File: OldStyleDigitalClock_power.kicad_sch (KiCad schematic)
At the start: 23 parts, among them J1 USB_A_OUT, J2 USB_A_OUT, J3 USB_C_IN, U11 NA555P

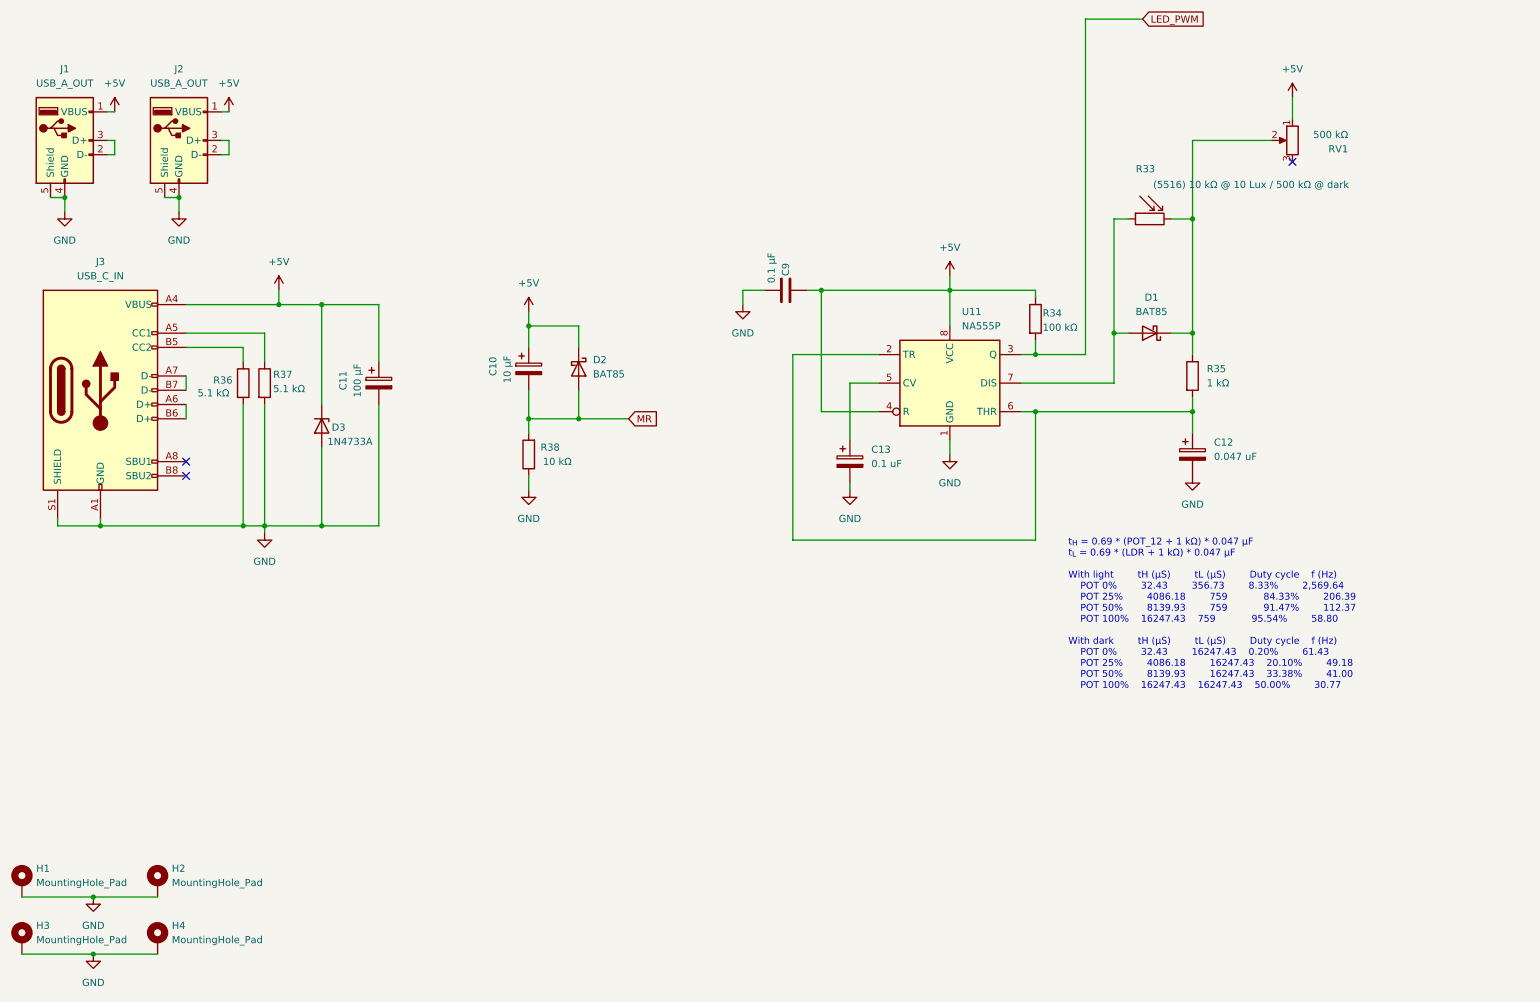
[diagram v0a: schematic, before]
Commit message: Constant frequency PWM with fixed LDR value
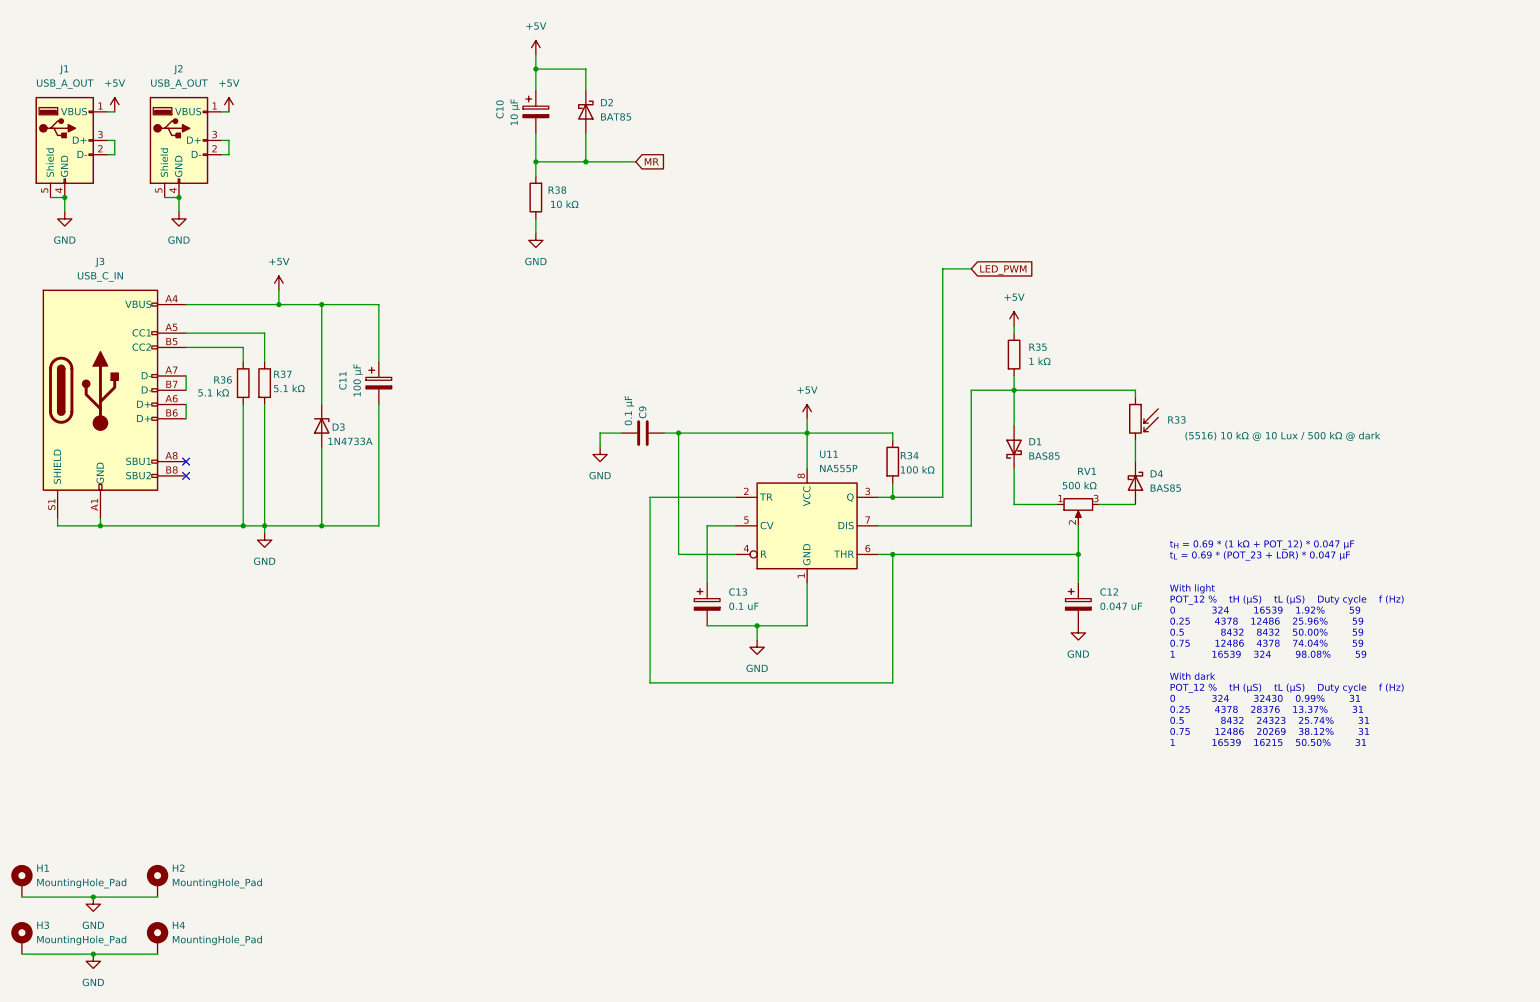
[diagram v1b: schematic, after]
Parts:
- added D4: BAS85, Diode_THT:D_DO-35_SOD27_P7.62mm_Horizontal, symbol Diode:BAT85
- D1: value BAT85 -> BAS85
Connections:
- net +5V: now also R35.1; no longer RV1.1
- net at C12.1, U11.2 (TR), U11.6 (THR): now also RV1.2; no longer R35.2
- net at RV1.3: now also D4.2 (A)
- net at D1.2 (A), R33.1, U11.7 (DIS): now also R35.2
- new net: D1.1 (K), RV1.1
- new net: D4.1 (K), R33.2
- no-connect marks 3 -> 2
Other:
- note added: "t_{H} = 0.69 * (1 kΩ + POT_12) * 0.047 µF t_{L} = 0.69 * (POT_23 + LDR) * 0.047 µF With light POT_12 % tH (µS) tL (µS) Duty cycle f (Hz) 0 324 16539 1.92% 59 0.25 4378 12486 25.96% 59 0.5 8432 8432 50.00% 59 0.75 12486 4378 74.04% 59 1 16539 324 98.08% 59 With dark POT_12 % tH (µS) tL (µS) Duty cycle f (Hz) 0 324 32430 0.99% 31 0.25 4378 28376 13.37% 31 0.5 8432 24323 25.74% 31 0.75 12486 20269 3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"
- note removed: "t_{H} = 0.69 * (POT_12 + 1 kΩ) * 0.047 µF t_{L} = 0.69 * (LDR + 1 kΩ) * 0.047 µF With light tH (µS) tL (µS) Duty cycle f (Hz) POT 0% 32.43 356.73 8.33% 2,569.64 POT 25% 4086.18 759 84.33% 206.39 POT 50% 8139.93 759 91.47% 112.37 POT 100% 16247.43 759 95.54% 58.80 With dark tH (µS) tL (µS) Duty cycle f (Hz) POT 0% 32.43 16247.43 0.20% 61.43 POT 25% 4086.18 16247.43 20.10% 49.18 POT 50% 8139.93 162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"
- moved on the sheet: C10, C12, C13, C9, D1, D2, R33, R34, R35, R38, RV1, U11

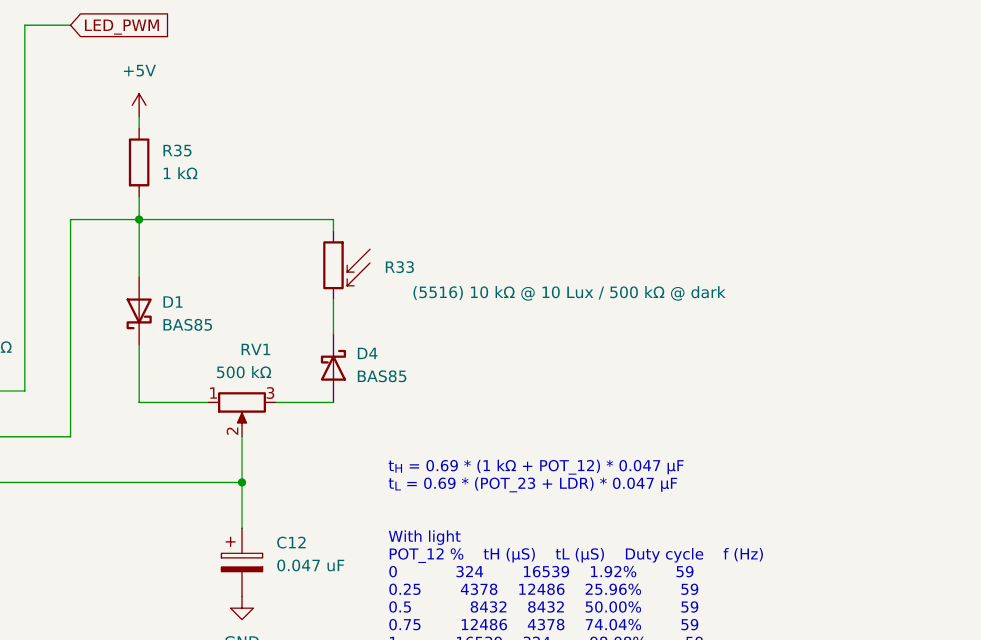
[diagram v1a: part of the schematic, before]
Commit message: Fixed typo
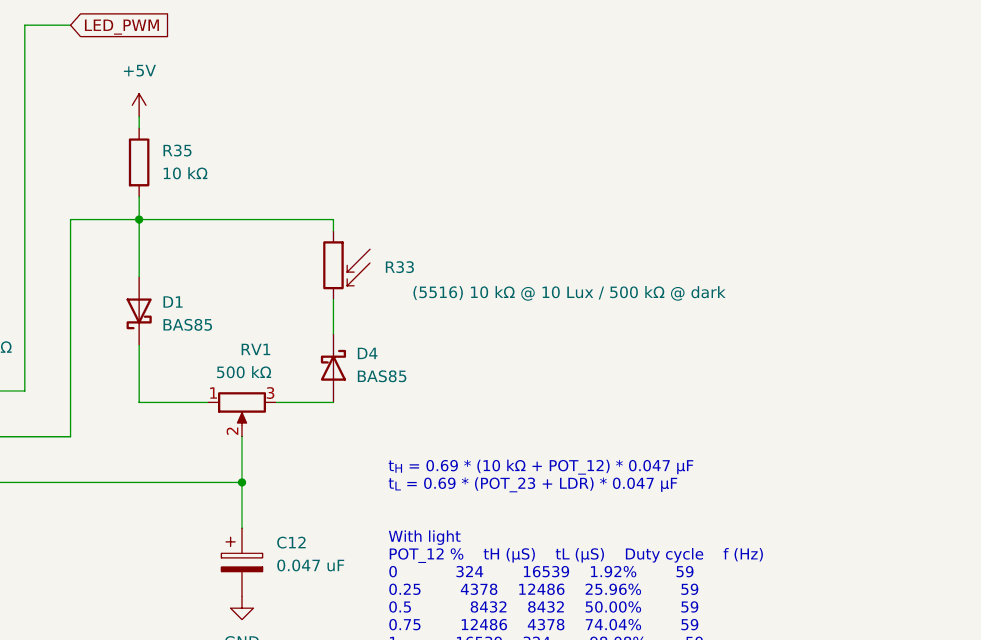
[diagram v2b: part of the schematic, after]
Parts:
- R35: value 1 kΩ -> 10 kΩ
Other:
- note added: "t_{H} = 0.69 * (10 kΩ + POT_12) * 0.047 µF t_{L} = 0.69 * (POT_23 + LDR) * 0.047 µF With light POT_12 % tH (µS) tL (µS) Duty cycle f (Hz) 0 324 16539 1.92% 59 0.25 4378 12486 25.96% 59 0.5 8432 8432 50.00% 59 0.75 12486 4378 74.04% 59 1 16539 324 98.08% 59 With dark POT_12 % tH (µS) tL (µS) Duty cycle f (Hz) 0 324 32430 0.99% 31 0.25 4378 28376 13.37% 31 0.5 8432 24323 25.74% 31 0.75 12486 20269 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"
- note removed: "t_{H} = 0.69 * (1 kΩ + POT_12) * 0.047 µF t_{L} = 0.69 * (POT_23 + LDR) * 0.047 µF With light POT_12 % tH (µS) tL (µS) Duty cycle f (Hz) 0 324 16539 1.92% 59 0.25 4378 12486 25.96% 59 0.5 8432 8432 50.00% 59 0.75 12486 4378 74.04% 59 1 16539 324 98.08% 59 With dark POT_12 % tH (µS) tL (µS) Duty cycle f (Hz) 0 324 32430 0.99% 31 0.25 4378 28376 13.37% 31 0.5 8432 24323 25.74% 31 0.75 12486 20269 3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"
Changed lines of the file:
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@@
 		(company "Pasquale Lafiosca")
 	)
-	(text "t_{H} = 0.69 * (1 kΩ + POT_12) * 0.047 µF\nt_{L} = 0.69 * (POT_23 + LDR) * 0.047 µF\n\n\nWith light				\nPOT_12 %	tH (µS)	tL (µS)	Duty cycle	f (Hz)\n0			324		16539	1.92%		59\n0.25		4378	12486	25.96%		59\n0.5			8432	8432	50.00%		59\n0.75		12486	4378	74.04%		59\n1			16539	324		98.08%		59\n				\nWith dark				\nPOT_12 %	tH (µS)	tL (µS)	Duty cycle	f (Hz)\n0			324		32430	0.99%		31\n0.25		4378	28376	13.37%		31\n0.5			8432	24323	25.74%		31\n0.75		12486	20269	38.12%		31\n1			16539	16215	50.50%		31\n"
+	(text "t_{H} = 0.69 * (10 kΩ + POT_12) * 0.047 µF\nt_{L} = 0.69 * (POT_23 + LDR) * 0.047 µF\n\n\nWith light				\nPOT_12 %	tH (µS)	tL (µS)	Duty cycle	f (Hz)\n0			324		16539	1.92%		59\n0.25		4378	12486	25.96%		59\n0.5			8432	8432	50.00%		59\n0.75		12486	4378	74.04%		59\n1			16539	324		98.08%		59\n				\nWith dark				\nPOT_12 %	tH (µS)	tL (µS)	Duty cycle	f (Hz)\n0			324		32430	0.99%		31\n0.25		4378	28376	13.37%		31\n0.5			8432	24323	25.74%		31\n0.75		12486	20269	38.12%		31\n1			16539	16215	50.50%		31\n"
 		(exclude_from_sim no)
 		(at 229.616 112.014 0)
@@
 			)
 		)
-		(property "Value" "1 kΩ"
+		(property "Value" "10 kΩ"
 			(at 204.47 80.0099 0)
 			(effects

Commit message: Assigned footprints: first draft
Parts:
- removed U11: NA555P, Package_DIP:DIP-8_W7.62mm, symbol Timer:NA555P
- added U12: NE555D, Package_SO:SOIC-8_3.9x4.9mm_P1.27mm, symbol Timer:NE555D
- RV1: footprint Resistor_SMD:R_1206_3216Metric -> Potentiometer_THT:Potentiometer_Alps_RK163_Single_Horizontal
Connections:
- net +5V: now also U12.4 (R), U12.8 (VCC)
- net GND: now also U12.1 (GND)
- net LED_PWM: now also U12.3 (Q)
- net at C12.1, RV1.2: now also U12.2 (TR), U12.6 (THR)
- net at D1.2 (A), R33.1, R35.2: now also U12.7 (DIS)
- net at C13.1: now also U12.5 (CV)
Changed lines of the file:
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@@
 			)
 		)
-		(property "Footprint" "Resistor_SMD:R_1206_3216Metric"
+		(property "Footprint" "Potentiometer_THT:Potentiometer_Alps_RK163_Single_Horizontal"
 			(at 213.36 105.41 0)
 			(effects
@@
 	)
 	(symbol
-		(lib_id "Timer:NA555P")
-		(at 165.1 109.22 0)
-		(unit 1)
-		(exclude_from_sim no)
-		(in_bom yes)
-		(on_board yes)
-		(dnp no)
-		(fields_autoplaced yes)
-		(property "Reference" "U11"
-			(at 167.2433 96.52 0)
-			(effects
-				(font
-					(size 1.27 1.27)
-				)
-				(justify left)
-			)
-		)
-		(property "Value" "NA555P"
-			(at 167.2433 99.06 0)
-			(effects
-				(font
-					(size 1.27 1.27)
-				)
-				(justify left)
-			)
-		)
-		(property "Footprint" "Package_DIP:DIP-8_W7.62mm"
-			(at 181.61 119.38 0)
-			(effects
-				(font
-					(size 1.27 1.27)
-				)
-				(hide yes)
-			)
-		)
-		(property "Datasheet" "http://www.ti.com/lit/ds/symlink/ne555.pdf"
-			(at 186.69 119.38 0)
-			(effects
-				(font
-					(size 1.27 1.27)
-				)
-				(hide yes)
-			)
-		)
-		(property "Description" "Precision Timers, 555 compatible, PDIP-8"
-			(at 165.1 109.22 0)
-			(effects
-				(font
-					(size 1.27 1.27)
-				)
-				(hide yes)
-			)
-		)
-		(pin "1"
-		)
-		(pin "4"
-		)
-		(pin "5"
-		)
-		(pin "8"
-		)
-		(pin "2"
-		)
-		(pin "3"
-		)
-		(pin "6"
-		)
-		(pin "7"
-		)
-		(instances
-			(project "OldStyleDigitalClock"
-				(path "/a24f1d5b-eb61-47a3-9a92-6515e74f7a21/31b03831-3d01-49ef-8f86-173fa6c5d953"
-					(reference "U11")
-					(unit 1)
-				)
-			)
-		)
-	)
-	(symbol
 		(lib_id "Device:C_Polarized")
 		(at 116.84 35.56 0)
@@
 					(unit 1)
 				)
+			)
+		)
+	)
+	(symbol
+		(lib_id "Timer:NE555D")
+		(at 165.1 109.22 0)
+		(unit 1)
+		(exclude_from_sim no)
+		(in_bom yes)
+		(on_board yes)
+		(dnp no)
+		(fields_autoplaced yes)
+		(property "Reference" "U12"
+			(at 167.2433 96.52 0)
+			(effects
+				(font
+					(size 1.27 1.27)
+				)
+				(justify left)
+			)
+		)
+		(property "Value" "NE555D"
+			(at 167.2433 99.06 0)
+			(effects
+				(font
+					(size 1.27 1.27)
+				)
+				(justify left)
+			)
+		)
+		(property "Footprint" "Package_SO:SOIC-8_3.9x4.9mm_P1.27mm"
+			(at 186.69 119.38 0)
+			(effects
+				(font
+					(size 1.27 1.27)
+				)
+				(hide yes)
+			)
+		)
+		(property "Datasheet" "http://www.ti.com/lit/ds/symlink/ne555.pdf"
+			(at 186.69 119.38 0)
+			(effects
+				(font
+					(size 1.27 1.27)
+				)
+				(hide yes)
+			)
+		)
+		(property "Description" "Precision Timers, 555 compatible, SOIC-8"
+			(at 165.1 109.22 0)
+			(effects
+				(font
+					(size 1.27 1.27)
+				)
+				(hide yes)
+			)
+		)
+		(pin "6"
+		)
+		(pin "1"
+		)
+		(pin "7"
+		)
+		(pin "3"
+		)
+		(pin "2"
+		)
+		(pin "8"
+		)
+		(pin "5"
+		)
+		(pin "4"
+		)
+		(instances
+			(project ""
+				(path "/a24f1d5b-eb61-47a3-9a92-6515e74f7a21/31b03831-3d01-49ef-8f86-173fa6c5d953"
+					(reference "U12")
+					(unit 1)
+				)
